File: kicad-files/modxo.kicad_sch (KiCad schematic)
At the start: 10 parts, among them J1 Conn_02x06_Odd_Even, J2 Conn_01x01_Pin, SW1 SW_DPDT_x2, U1 rp2040-zero

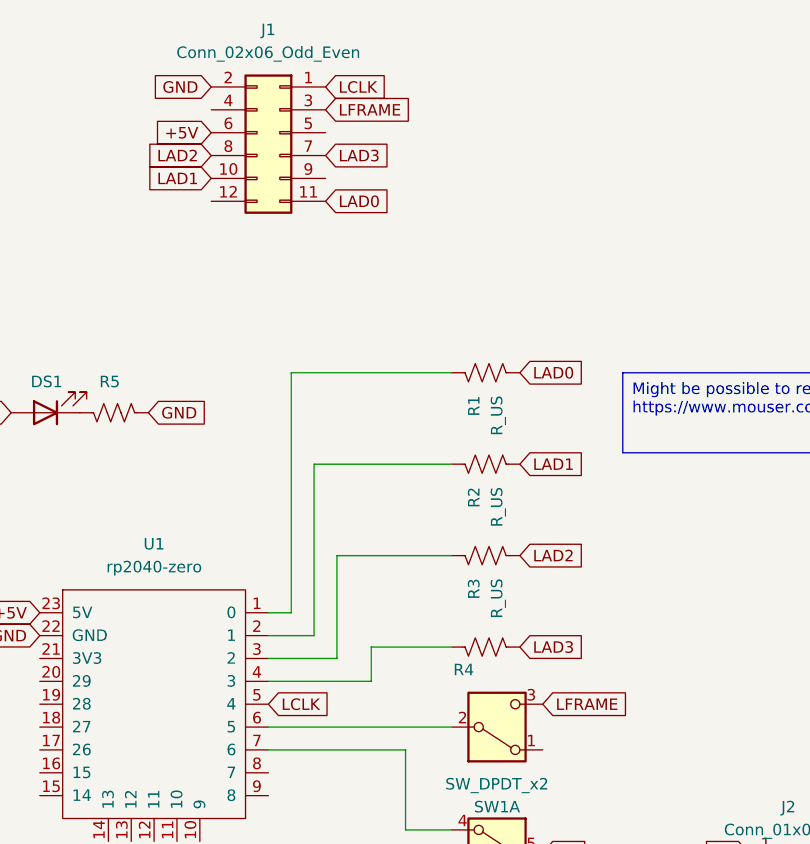
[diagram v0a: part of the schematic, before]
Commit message: Minor usability improvements
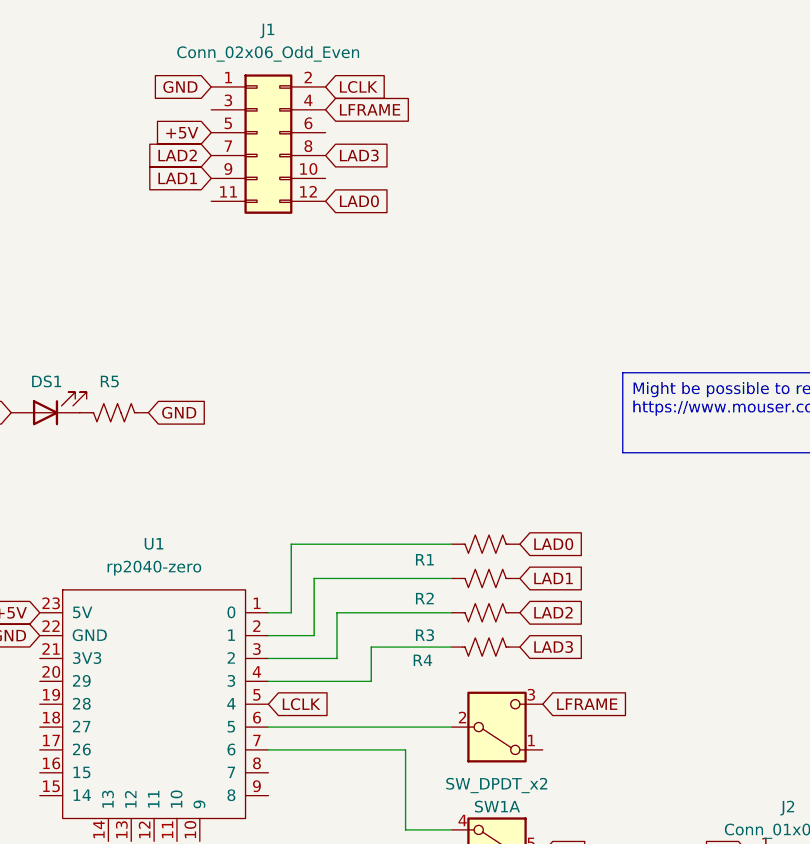
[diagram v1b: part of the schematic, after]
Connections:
- net +5V: now also J1.5 (Pin_5); no longer J1.6 (Pin_6)
- net GND: now also J1.1 (Pin_1); no longer J1.2 (Pin_2)
- net LAD0: now also J1.12 (Pin_12); no longer J1.11 (Pin_11)
- net LAD1: now also J1.9 (Pin_9); no longer J1.10 (Pin_10)
- net LAD2: now also J1.7 (Pin_7); no longer J1.8 (Pin_8)
- net LAD3: now also J1.8 (Pin_8); no longer J1.7 (Pin_7)
- net LCLK: now also J1.2 (Pin_2); no longer J1.1 (Pin_1)
- net LFRAME: now also J1.4 (Pin_4); no longer J1.3 (Pin_3)
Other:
- moved on the sheet: R1, R2, R3
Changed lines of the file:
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@@
 	(wire
 		(pts
-			(xy 146.05 106.68) (xy 146.05 118.11)
-		)
-		(stroke
-			(width 0)
-			(type default)
-		)
-	)
-	(wire
-		(pts
-			(xy 158.75 106.68) (xy 146.05 106.68)
+			(xy 146.05 113.03) (xy 146.05 118.11)
+		)
+		(stroke
+			(width 0)
+			(type default)
+		)
+	)
+	(wire
+		(pts
+			(xy 158.75 113.03) (xy 146.05 113.03)
 		)
 		(stroke
@@
 	(wire
 		(pts
-			(xy 140.97 86.36) (xy 140.97 113.03)
+			(xy 140.97 105.41) (xy 140.97 113.03)
 		)
 		(stroke
@@
 	(wire
 		(pts
-			(xy 158.75 96.52) (xy 143.51 96.52)
+			(xy 158.75 109.22) (xy 143.51 109.22)
 		)
 		(stroke
@@
 	(wire
 		(pts
-			(xy 158.75 86.36) (xy 140.97 86.36)
-		)
-		(stroke
-			(width 0)
-			(type default)
-		)
-	)
-	(wire
-		(pts
-			(xy 143.51 96.52) (xy 143.51 115.57)
+			(xy 158.75 105.41) (xy 140.97 105.41)
+		)
+		(stroke
+			(width 0)
+			(type default)
+		)
+	)
+	(wire
+		(pts
+			(xy 143.51 109.22) (xy 143.51 115.57)
 		)
 		(stroke
@@
 	(global_label "LAD0"
 		(shape input)
-		(at 166.37 86.36 0)
+		(at 166.37 105.41 0)
 		(fields_autoplaced yes)
 		(effects
@@
 		)
 		(property "Intersheetrefs" "${INTERSHEET_REFS}"
-			(at 173.9514 86.36 0)
+			(at 173.9514 105.41 0)
 			(effects
 				(font
@@
 	(global_label "LAD1"
 		(shape input)
-		(at 166.37 96.52 0)
+		(at 166.37 109.22 0)
 		(fields_autoplaced yes)
 		(effects
@@
 		)
 		(property "Intersheetrefs" "${INTERSHEET_REFS}"
-			(at 173.9514 96.52 0)
+			(at 173.9514 109.22 0)
 			(effects
 				(font
@@
 	(global_label "LAD2"
 		(shape input)
-		(at 166.37 106.68 0)
+		(at 166.37 113.03 0)
 		(fields_autoplaced yes)
 		(effects
@@
 		)
 		(property "Intersheetrefs" "${INTERSHEET_REFS}"
-			(at 173.9514 106.68 0)
+			(at 173.9514 113.03 0)
 			(effects
 				(font
@@
 	(symbol
 		(lib_id "Device:R_US")
-		(at 162.56 106.68 90)
+		(at 162.56 113.03 90)
 		(mirror x)
 		(unit 1)
@@
 		(on_board yes)
 		(dnp no)
-		(fields_autoplaced yes)
 		(property "Reference" "R3"
-			(at 161.2899 109.22 0)
+			(at 156.972 115.57 90)
 			(effects
 				(font
@@
 		)
 		(property "Value" "R_US"
-			(at 163.8299 109.22 0)
-			(effects
-				(font
-					(size 1.27 1.27)
-				)
-				(justify left)
+			(at 163.8299 115.57 0)
+			(effects
+				(font
+					(size 1.27 1.27)
+				)
+				(justify left)
+				(hide yes)
 			)
 		)
 		(property "Footprint" "Resistor_SMD:R_0805_2012Metric_Pad1.20x1.40mm_HandSolder"
-			(at 162.814 107.696 90)
+			(at 162.814 114.046 90)
 			(effects
 				(font
@@
 		)
 		(property "Datasheet" "~"
-			(at 162.56 106.68 0)
+			(at 162.56 113.03 0)
 			(effects
 				(font
@@
 		)
 		(property "Description" "Resistor, US symbol"
-			(at 162.56 106.68 0)
+			(at 162.56 113.03 0)
 			(effects
 				(font
@@
 	(symbol
 		(lib_id "Connector_Generic:Conn_02x06_Odd_Even")
-		(at 139.7 59.69 0)
-		(mirror y)
+		(at 137.16 59.69 0)
 		(unit 1)
 		(exclude_from_sim no)
@@
 		(on_board yes)
 		(dnp no)
-		(fields_autoplaced yes)
 		(property "Reference" "J1"
 			(at 138.43 48.26 0)
@@
 		)
 		(property "Footprint" "Connector_PinHeader_2.54mm:PinHeader_2x06_P2.54mm_Vertical"
-			(at 139.7 59.69 0)
+			(at 137.16 59.69 0)
 			(effects
 				(font
@@
 		)
 		(property "Datasheet" "~"
-			(at 139.7 59.69 0)
+			(at 137.16 59.69 0)
 			(effects
 				(font
@@
 		)
 		(property "Description" "Generic connector, double row, 02x06, odd/even pin numbering scheme (row 1 odd numbers, row 2 even numbers), script generated (kicad-library-utils/schlib/autogen/connector/)"
-			(at 139.7 59.69 0)
+			(at 137.16 59.69 0)
 			(effects
 				(font
@@
 	(symbol
 		(lib_id "Device:R_US")
-		(at 162.56 96.52 90)
+		(at 162.56 109.22 90)
 		(mirror x)
 		(unit 1)
@@
 		(on_board yes)
 		(dnp no)
-		(fields_autoplaced yes)
 		(property "Reference" "R2"
-			(at 161.2899 99.06 0)
+			(at 156.972 111.506 90)
 			(effects
 				(font
@@
 		)
 		(property "Value" "R_US"
-			(at 163.8299 99.06 0)
-			(effects
-				(font
-					(size 1.27 1.27)
-				)
-				(justify left)
+			(at 163.8299 111.76 0)
+			(effects
+				(font
+					(size 1.27 1.27)
+				)
+				(justify left)
+				(hide yes)
 			)
 		)
 		(property "Footprint" "Resistor_SMD:R_0805_2012Metric_Pad1.20x1.40mm_HandSolder"
-			(at 162.814 97.536 90)
+			(at 162.814 110.236 90)
 			(effects
 				(font
@@
 		)
 		(property "Datasheet" "~"
-			(at 162.56 96.52 0)
+			(at 162.56 109.22 0)
 			(effects
 				(font
@@
 		)
 		(property "Description" "Resistor, US symbol"
-			(at 162.56 96.52 0)
+			(at 162.56 109.22 0)
 			(effects
 				(font
@@
 		(dnp no)
 		(property "Reference" "R4"
-			(at 161.2899 119.38 90)
+			(at 156.718 118.364 90)
 			(effects
 				(font
@@
 	(symbol
 		(lib_id "Device:R_US")
-		(at 162.56 86.36 90)
+		(at 162.56 105.41 90)
 		(mirror x)
 		(unit 1)
@@
 		(on_board yes)
 		(dnp no)
-		(fields_autoplaced yes)
 		(property "Reference" "R1"
-			(at 161.2899 88.9 0)
+			(at 156.972 107.188 90)
 			(effects
 				(font
@@
 		)
 		(property "Value" "R_US"
-			(at 163.8299 88.9 0)
-			(effects
-				(font
-					(size 1.27 1.27)
-				)
-				(justify left)
+			(at 163.83 99.06 90)
+			(effects
+				(font
+					(size 1.27 1.27)
+				)
+				(justify left)
+				(hide yes)
 			)
 		)
 		(property "Footprint" "Resistor_SMD:R_0805_2012Metric_Pad1.20x1.40mm_HandSolder"
-			(at 162.814 87.376 90)
+			(at 162.814 106.426 90)
 			(effects
 				(font
@@
 		)
 		(property "Datasheet" "~"
-			(at 162.56 86.36 0)
+			(at 162.56 105.41 0)
 			(effects
 				(font
@@
 		)
 		(property "Description" "Resistor, US symbol"
-			(at 162.56 86.36 0)
-			(effects
-				(font
+			(at 162.56 105.41 0)
+			(effects
+				(font
